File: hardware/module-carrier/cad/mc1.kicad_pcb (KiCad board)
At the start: 2 copper layers, 65 x 75 mm, 21 parts, among them J1 FUSED ISOLATED 5V INPUT, J2 D24V22F3 external assembled b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, J3 DFR0627 WK2132 ready module h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, J4 ZAC93 ready module harness, J5 CC1101 ready module harness, J6 LD2450 radar harness, J7 BME680 external pod harness, J8 XIAO BOOT unpopulated service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, J9 Nano BOOT unpopulated service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, U1 Waveshare ESP32-S3-Nano-M 16M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, U2 ESP32-H2-DevKitM-1-N4S, U3 Seeed XIAO MG24 pre-soldered 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, U4 WIZ850io finished module

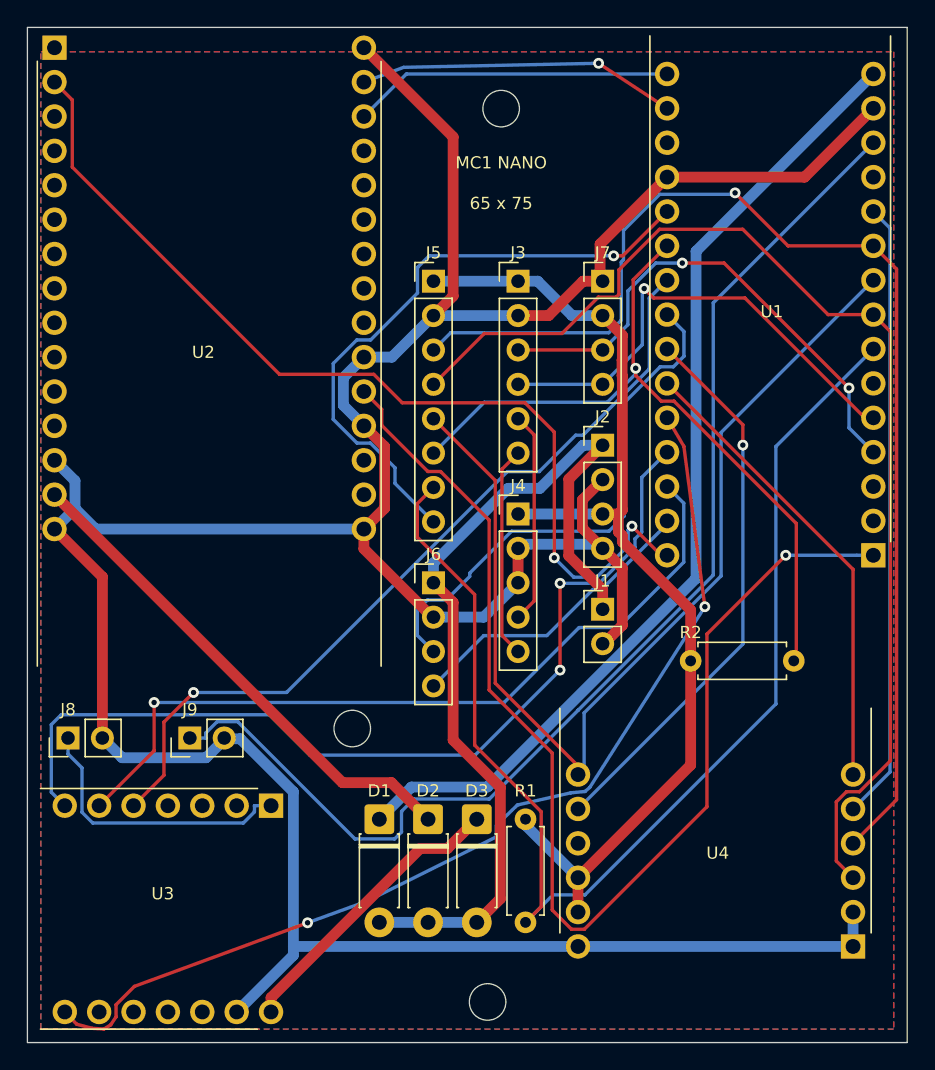
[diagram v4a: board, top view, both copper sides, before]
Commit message: Compact MC1 to 51x75 with ceiling-side Ethernet and headers
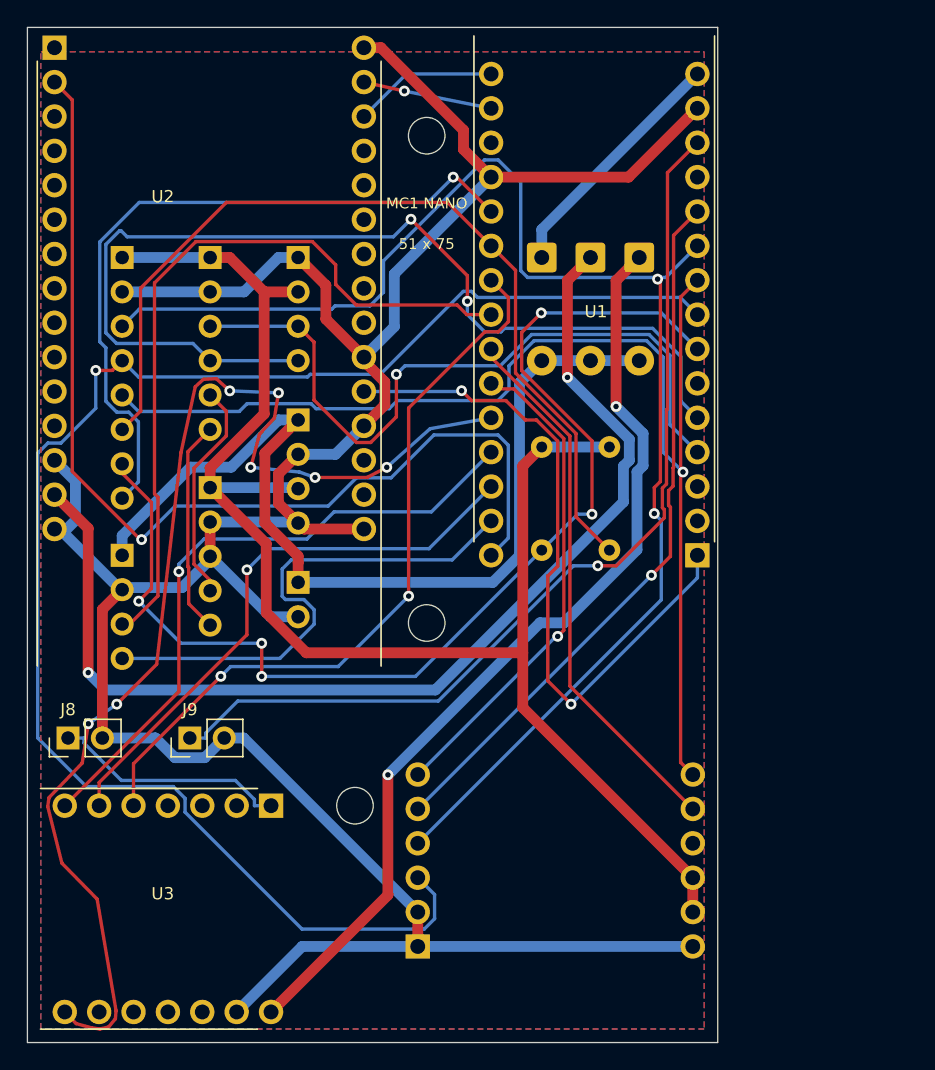
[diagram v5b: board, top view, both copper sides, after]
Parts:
- D1, D2, D3, J1, J2, J3, J4, J5, J6, J7, R1, R2, U4: moved to B.Cu
- moved D1 43.2 mm to (38.0, 17.0)
- moved D2 43.2 mm to (41.6, 17.0)
- moved D3 43.2 mm to (45.2, 17.0)
- moved U4 32.2 mm to (28.8, 67.9), turned to 0 degrees
- moved R1 27.5 mm to (38.0, 31.0)
- moved J6 23.1 mm to (7.00, 39.0), turned to 180 degrees
- moved J5 23.1 mm to (7.00, 17.0), turned to 180 degrees
- moved J4 22.8 mm to (13.5, 34.0), turned to 180 degrees
- moved J3 22.8 mm to (13.5, 17.0), turned to 180 degrees
- moved J1 22.6 mm to (20.0, 41.0), turned to 180 degrees
- moved J2 22.6 mm to (20.0, 29.0), turned to 180 degrees
- moved J7 22.6 mm to (20.0, 17.0), turned to 180 degrees
- moved H3 17.5 mm to (24.2, 57.5)
- moved R2 16.9 mm to (43.0, 31.0), turned to -90 degrees
- moved U1 13.0 mm to (49.5, 39.0)
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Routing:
- net /+5V_S3: track 73.5 -> 18.3 mm
- net /+5V_ZB: track 21.7 -> 69.7 mm, vias 0 -> 2
- net /+5V_H2: track 37.5 -> 80.8 mm, vias 0 -> 2
- net /I2C_SCL: track 35.5 -> 76.3 mm, vias 1 -> 2
- net /THREAD_BOOT: track 87.8 -> 51.2 mm, vias 1 -> 2
- net /GND: track 249.2 -> 213.5 mm
- net /+3V3: track 77.4 -> 113.0 mm
- net /SPI_MOSI: track 85.8 -> 117.7 mm, vias 0 -> 1
- net /ZB_TX: track 69.2 -> 47.8 mm, vias 2 -> 1
- net /SPI_SCK: track 88.9 -> 107.1 mm, vias 1 -> 2
- net /S3_BOOT_SERVICE: track 88.8 -> 70.9 mm, vias 0 -> 1
- net /ZB_RTS: track 58.8 -> 42.5 mm
- net /RADAR_RX: track 39.7 -> 55.9 mm
- net /I2C_SDA: track 37.9 -> 53.8 mm, vias 2 -> 1
- net /RADAR_TX: track 22.4 -> 38.0 mm
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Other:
- board size 65 x 75 mm -> 51 x 75 mm
- board text added: "51 x 75"
- board text removed: "65 x 75"

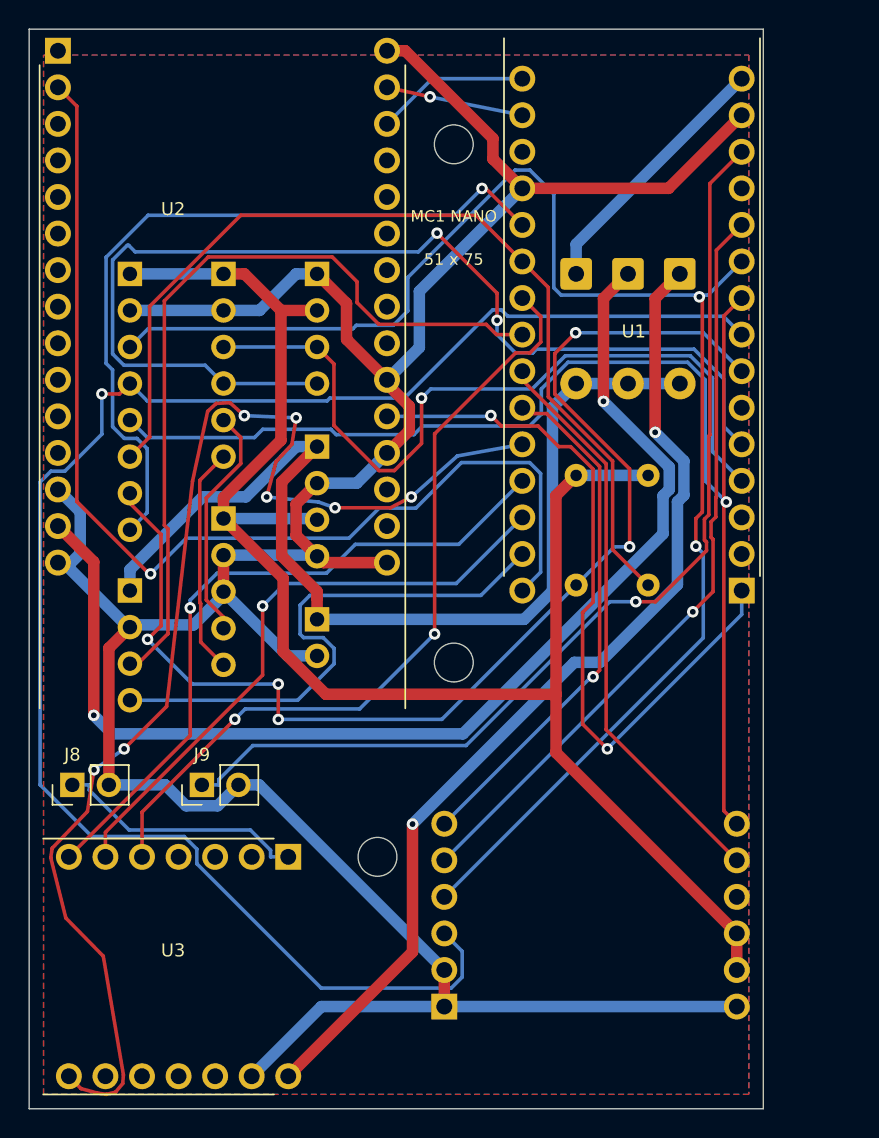
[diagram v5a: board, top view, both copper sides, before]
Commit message: Support RJ45 on both sides and optimize MC1 component routing
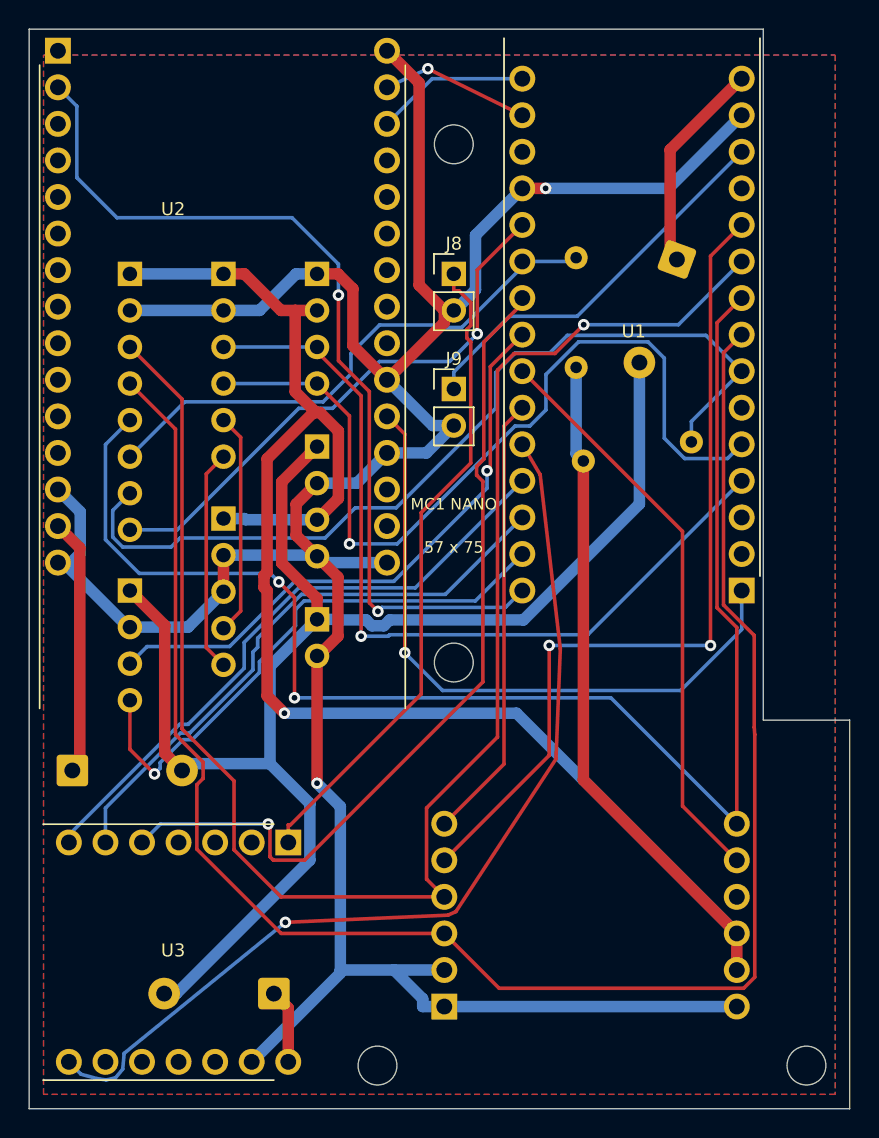
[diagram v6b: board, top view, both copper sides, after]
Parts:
- added H4: M2.5 NYLON NPTH, , F.Cu at (54.0, 72.0)
- moved D3 57.4 mm to (17.0, 67.0), turned to 180 degrees
- moved D2 51.8 mm to (3.00, 51.5), turned to 0 degrees
- moved J8 44.3 mm to (29.5, 17.0), turned to 0 degrees
- moved J9 32.6 mm to (29.5, 25.0), turned to 0 degrees
- moved H3 14.5 mm to (24.2, 72.0)
- moved R2 9.01 mm to (38.0, 23.5), turned to 90 degrees
- moved D1 7.07 mm to (45.0, 16.0), turned to -110 degrees
- moved R1 1.12 mm to (38.5, 30.0), turned to 10 degrees
- moved U3 1.00 mm to (18.0, 56.5)
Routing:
- net /+5V_ZB: track 69.7 -> 5.15 mm, vias 2 -> 0
- net /+5V_H2: track 80.8 -> 17.8 mm, vias 2 -> 0
- net /S3_BOOT_SERVICE: track 70.9 -> 27.5 mm, vias 1 -> 0
- net /+5V: track 71.5 -> 103.4 mm
- net /+3V3: track 113.0 -> 144.4 mm, vias 0 -> 1
- net /RF_CS: track 66.9 -> 37.9 mm
- net /ZB_BOOT_SERVICE: track 17.6 -> 45.8 mm
- net /RF_GDO0: track 83.9 -> 62.5 mm, vias 5 -> 0
- net /ZB_RX: track 88.0 -> 66.9 mm, vias 7 -> 1
- net /I2C_SCL: track 76.3 -> 60.1 mm, vias 2 -> 1
- net /RF_GDO2: track 53.1 -> 38.6 mm
- net /RADAR_RX: track 55.9 -> 41.5 mm, vias 0 -> 1
- net /THREAD_EN: track 75.8 -> 63.4 mm, vias 1 -> 2
- net /SPI_MISO: track 91.1 -> 102.9 mm, vias 1 -> 2
- net /ETH_CS: track 52.8 -> 59.3 mm, vias 1 -> 2
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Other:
- board size 51 x 75 mm -> 57 x 75 mm
- board text added: "57 x 75"
- board text removed: "51 x 75"

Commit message: Center Ethernet and enforce rear-first carrier assembly
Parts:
- moved H3 20.9 mm to (18.0, 52.0)
- moved U3 16.6 mm to (1.50, 58.3), turned to 0 degrees
- moved H4 6.00 mm to (48.0, 72.0)
- moved U4 6.00 mm to (22.8, 67.9)
- moved D3 4.92 mm to (12.5, 65.0)
- moved D2 0.70 mm to (3.00, 50.8)
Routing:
- net /+3V3: track 144.4 -> 115.4 mm
- net /SPI_MOSI: track 123.8 -> 103.4 mm, vias 0 -> 1
- net /THREAD_EN: track 63.4 -> 83.0 mm, vias 2 -> 1
- net /ZB_BOOT_SERVICE: track 45.8 -> 64.6 mm
- net /ZB_TX: track 43.3 -> 60.1 mm
- net /ZB_RTS: track 40.8 -> 57.4 mm
- net /ZB_RX: track 66.9 -> 52.7 mm, vias 1 -> 2
- net /GND: track 209.2 -> 195.6 mm, vias 2 -> 1
- net /I2C_SDA: track 58.8 -> 48.6 mm
- net /ETH_INT: track 31.1 -> 40.4 mm, vias 0 -> 1
- net /RF_GDO0: track 62.5 -> 53.6 mm, vias 0 -> 1
- net /I2C_SCL: track 60.1 -> 68.2 mm
- net /RADAR_TX: track 39.0 -> 31.9 mm, vias 1 -> 0
- net /THREAD_BOOT: track 45.9 -> 39.1 mm, vias 1 -> 0
- net /ZB_CTS: track 59.8 -> 66.1 mm, vias 1 -> 2
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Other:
- board size 57 x 75 mm -> 51 x 75 mm
- board text added: "51 x 75"
- board text removed: "57 x 75"

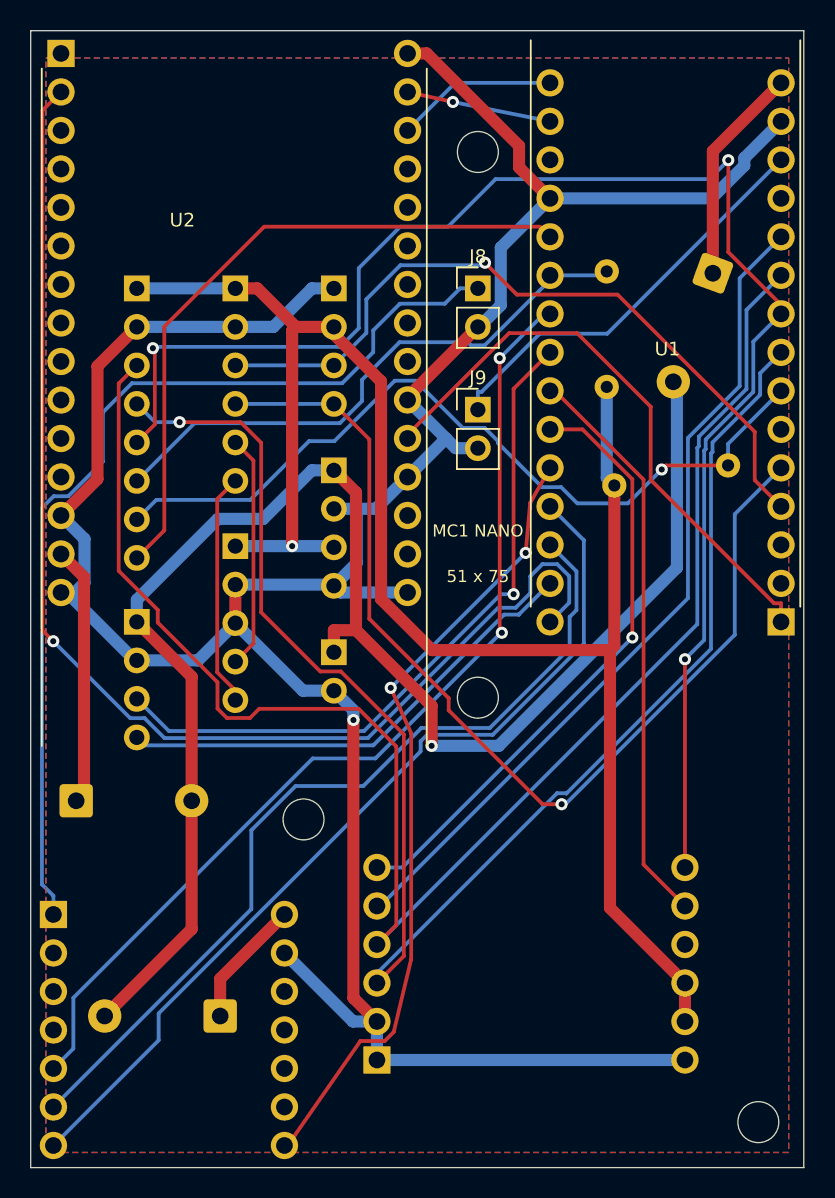
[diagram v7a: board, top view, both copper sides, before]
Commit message: Compact MC1 around one retainer and split enclosure rails
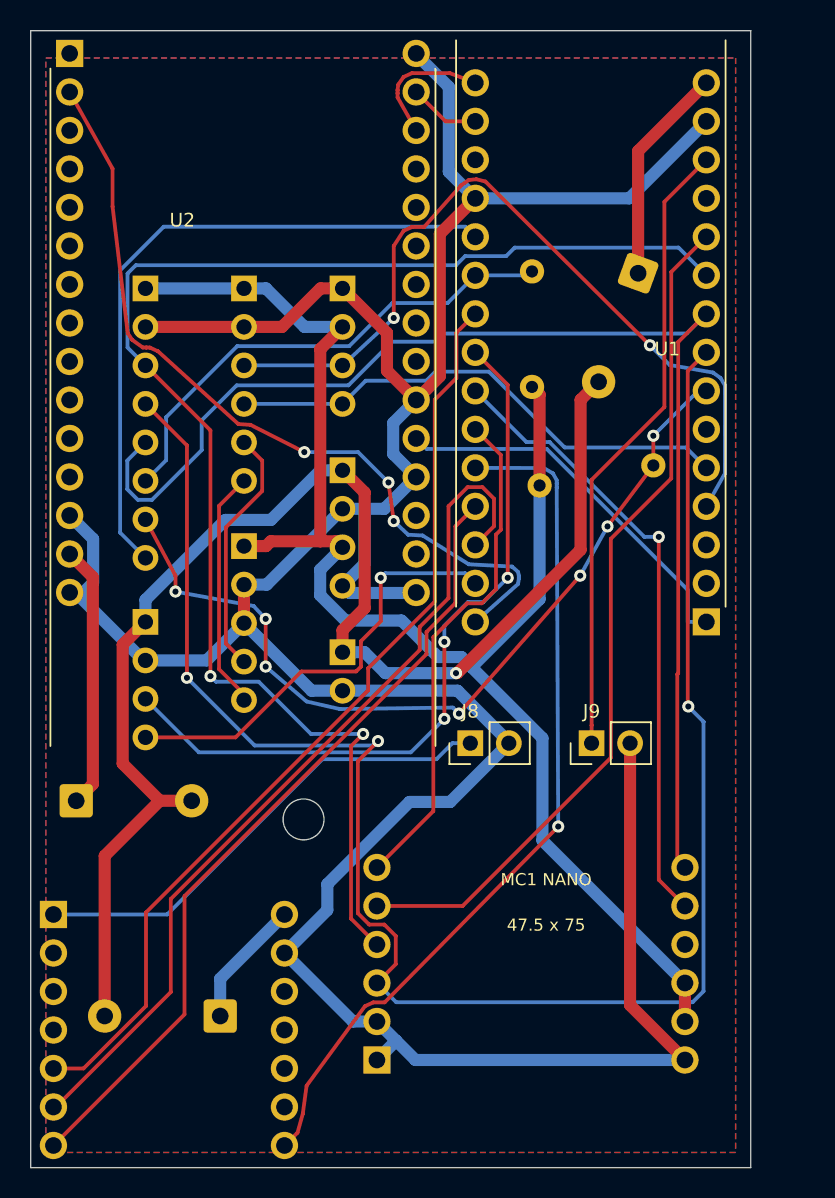
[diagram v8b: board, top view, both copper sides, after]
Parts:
- removed H1, H2, H4: M2.5 NYLON NPTH, 
- moved J8 30.0 mm to (29.0, 47.0), turned to 90 degrees
- moved J9 23.2 mm to (37.0, 47.0), turned to 90 degrees
- moved D1 4.93 mm to (40.1, 16.0)
- moved R1 4.93 mm to (33.6, 30.0)
- moved R2 4.93 mm to (33.1, 23.5)
- moved U1 4.93 mm to (44.6, 39.0)
- moved J1 0.57 mm to (20.6, 41.0)
- moved J2 0.57 mm to (20.6, 29.0)
- moved J3 0.57 mm to (14.1, 17.0)
- moved J4 0.57 mm to (14.1, 34.0)
- moved J5 0.57 mm to (7.57, 17.0)
- moved J6 0.57 mm to (7.57, 39.0)
- moved J7 0.57 mm to (20.6, 17.0)
- moved U2 0.57 mm to (2.57, 1.50)
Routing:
- net /I2C_SCL: track 68.2 -> 34.0 mm, vias 1 -> 0
- net /ZB_BOOT_SERVICE: track 64.6 -> 32.2 mm
- net /THREAD_EN: track 83.0 -> 53.9 mm, vias 1 -> 3
- net /GND: track 195.6 -> 217.4 mm, vias 1 -> 0
- net /SPI_MISO: track 102.9 -> 85.8 mm, vias 3 -> 0
- net /SPI_MOSI: track 103.4 -> 117.9 mm, vias 1 -> 3
- net /+3V3: track 115.4 -> 101.1 mm, vias 1 -> 0
- net /S3_BOOT_SERVICE: track 27.5 -> 41.6 mm
- net /THREAD_BOOT: track 39.1 -> 25.4 mm
- net /SPI_SCK: track 107.9 -> 95.1 mm, vias 0 -> 2
- net /+5V: track 105.0 -> 93.7 mm
- net /ETH_INT: track 40.4 -> 33.6 mm, vias 1 -> 0
- net /ZB_TX: track 60.1 -> 53.7 mm
- net /RF_CS: track 37.9 -> 32.9 mm
- net /THREAD_TX: track 9.60 -> 4.70 mm, vias 1 -> 0
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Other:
- board size 51 x 75 mm -> 47.5 x 75 mm
- board text added: "47.5 x 75"
- board text removed: "51 x 75"
